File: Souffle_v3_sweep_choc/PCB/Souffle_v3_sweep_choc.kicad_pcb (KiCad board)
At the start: 2 copper layers, 137.2 x 114.5 mm, 84 parts, among them J1 LED, J2 4PIN, J3 OLED, J4 Conn_01x01_Female, J5 Conn_01x01_Female, SW1 SW_PUSH, SW10 SW_PUSH, SW11 SW_PUSH, SW12 SW_PUSH, SW13 SW_PUSH, SW14 SW_PUSH, SW15 SW_PUSH, SW16 SW_PUSH, SW17 SW_PUSH, SW18 SW_PUSH, SW19 SW_PUSH, SW2 SW_PUSH, SW20 SW_PUSH, SW21 SW_PUSH, SW22 SW_PUSH, SW23 SW_PUSH, SW24 SW_PUSH, SW25 SW_PUSH, SW25b1 RotaryEncoder_Switch, SW26 SW_PUSH, SW27 SW_PUSH, SW28 SW_PUSH, SW29 SW_PUSH, SW3 SW_PUSH, SW30 SW_PUSH, SW31 SW_SPDT, SW4 SW_PUSH, SW5 SW_PUSH, SW6 SW_PUSH, SW7 SW_PUSH, SW8 SW_PUSH, SW9 SW_PUSH, U1 ProMicro

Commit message: Final Soufflé Choc PCB.
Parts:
- moved D29 14.0 mm to (161.4, 113.9), turned to 180 degrees
- moved D27 13.1 mm to (116.9, 112.3), turned to 180 degrees
- moved D28 11.9 mm to (139.2, 110.7), turned to 180 degrees
- moved D26 5.30 mm to (100.2, 117.1), turned to 180 degrees
- moved D3 5.05 mm to (152.5, 37.7)
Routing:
- net row4: track 18.3 -> 177.1 mm
- net col1: track 66.2 -> 208.1 mm, vias 0 -> 6
- net col0: track 83.1 -> 222.7 mm, vias 0 -> 6
- net col2: track 66.1 -> 196.8 mm, vias 0 -> 5
- net col3: track 66.5 -> 185.9 mm, vias 0 -> 5
- net col4: track 66.1 -> 162.4 mm, vias 0 -> 6
- net SW25A: track 91.9 -> 139.4 mm
- net ENCB: track 30.2 -> 72.9 mm
- net ENCA: track 33.2 -> 75.5 mm
- net RAW: track 55.4 -> 96.2 mm, vias 2 -> 5
- net DATA: track 21.0 -> 60.3 mm
- net row3: track 146.5 -> 185.0 mm
- net BAT: track 44.3 -> 80.9 mm
- net row2: track 145.1 -> 170.1 mm
- net row0: track 145.2 -> 164.5 mm
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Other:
- board size 137.2 x 114.5 mm -> 132.1 x 108 mm
- board text added: "POWER"
- board text added: "Soufflé Keyboard v3-sweep-choc by JCliment"
- board text removed: "Soufflé Keyboard v3-sweep by J Climent"

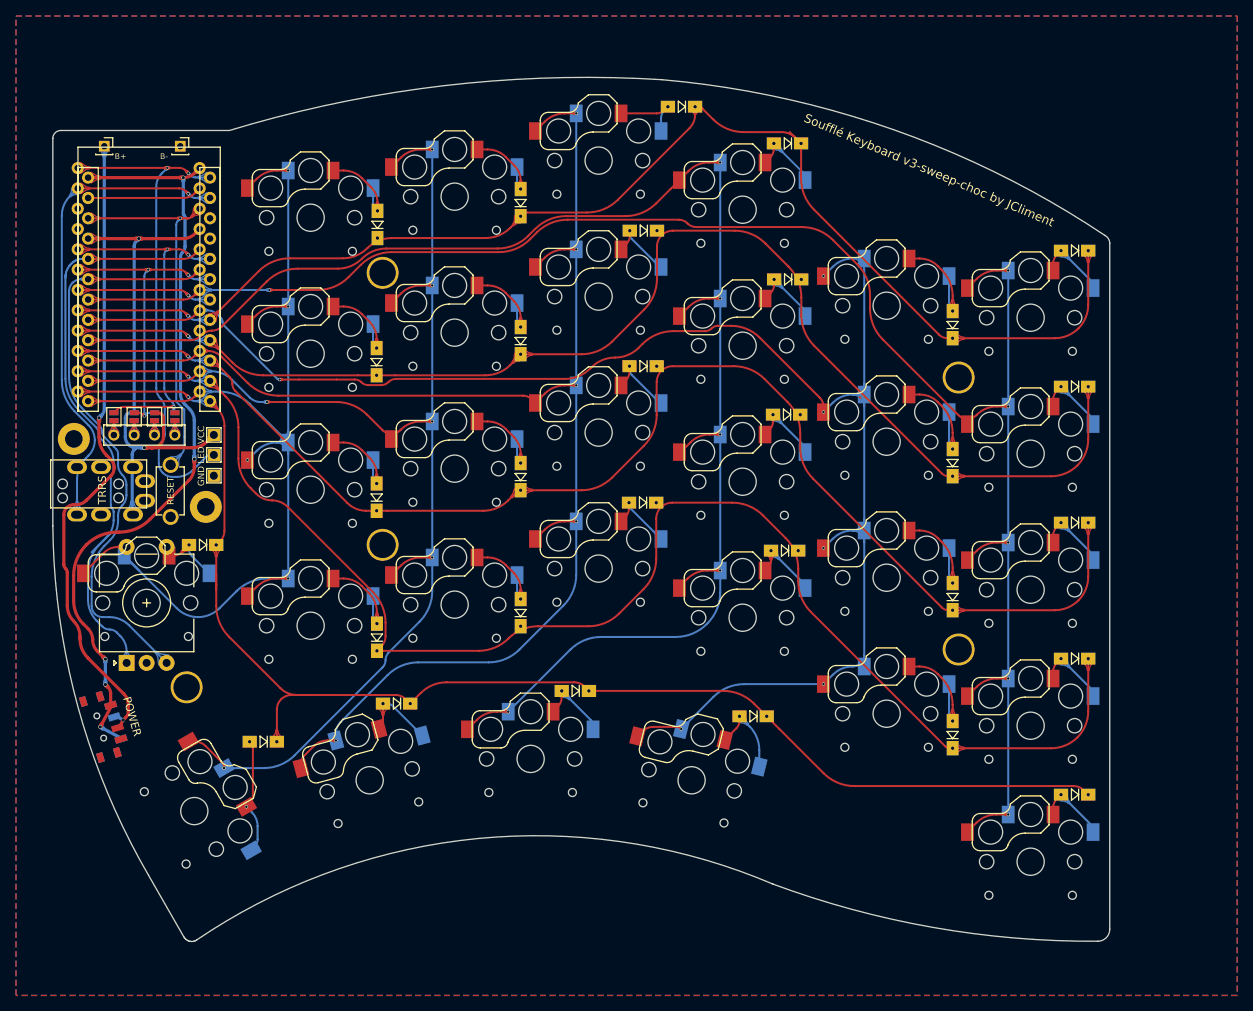
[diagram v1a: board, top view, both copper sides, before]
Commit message: Fixed horizontal spacing of the FN key.
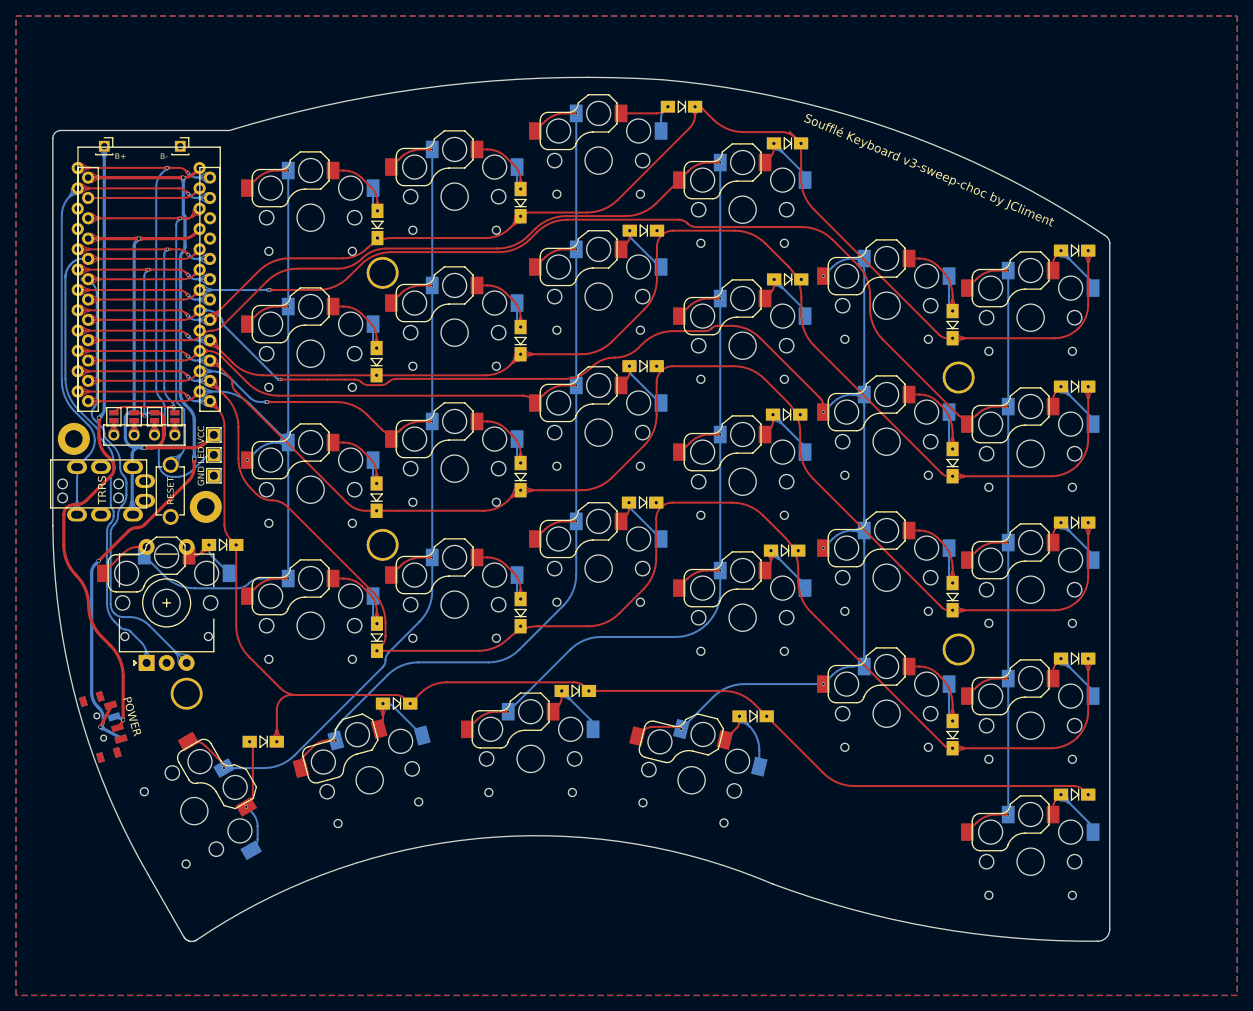
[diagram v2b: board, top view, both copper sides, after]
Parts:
- moved D25 2.50 mm to (95.1, 92.5)
- moved SW25 2.50 mm to (88.1, 99.7)
- moved SW25b1 2.50 mm to (85.6, 107.2)
- moved TH7 0.80 mm to (90.6, 111.1)
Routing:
- net SW25A: track 139.4 -> 132.2 mm
- net ENCA: track 75.5 -> 71.2 mm
- net ENCB: track 72.9 -> 70.0 mm
- net row4: track 177.1 -> 175.5 mm
- net BAT: track 80.9 -> 79.5 mm
- net RAW: track 96.2 -> 95.6 mm, vias 5 -> 4

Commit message: Final verifications and route cleaning.
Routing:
- net col1: track 208.1 -> 204.7 mm
- net row4: track 175.5 -> 172.3 mm
- net row0: track 164.5 -> 163.5 mm
- net row3: track 185.0 -> 185.9 mm
- net row2: track 170.1 -> 171.1 mm
- net row1: track 163.9 -> 164.8 mm
- net col3: track 185.9 -> 185.3 mm
